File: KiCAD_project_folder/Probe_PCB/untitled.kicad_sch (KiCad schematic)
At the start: 10 parts, among them U1 LTC2452ITS8-TRMPBF, U2 BMI160

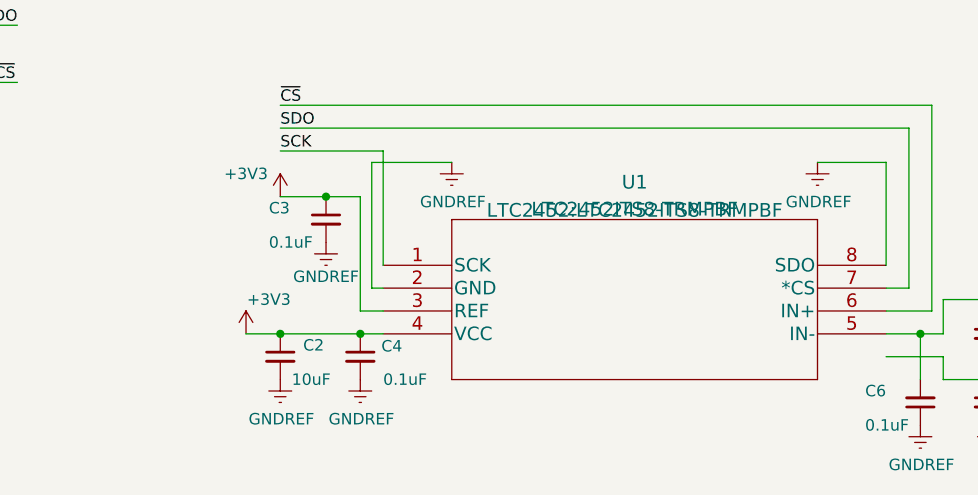
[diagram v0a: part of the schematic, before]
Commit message: Added draft PCB layout for probe
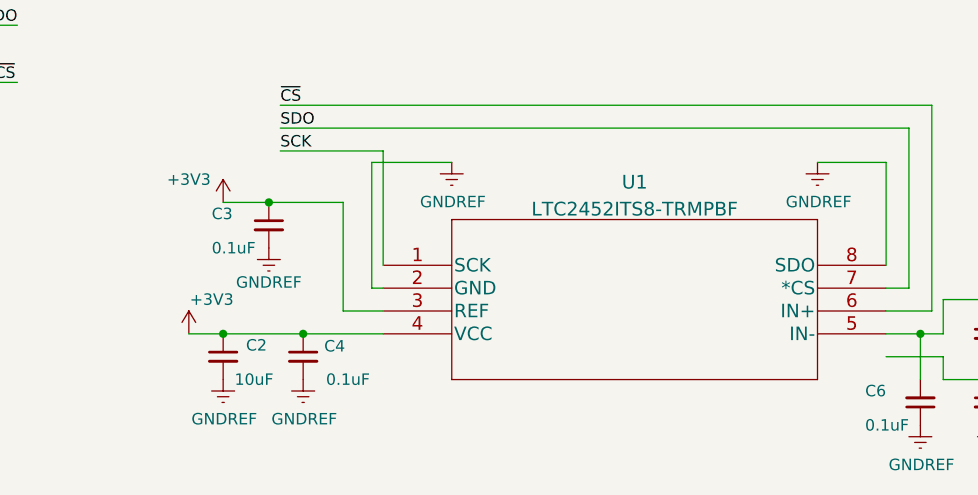
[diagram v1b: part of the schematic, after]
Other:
- moved on the sheet: C2, C3, C4

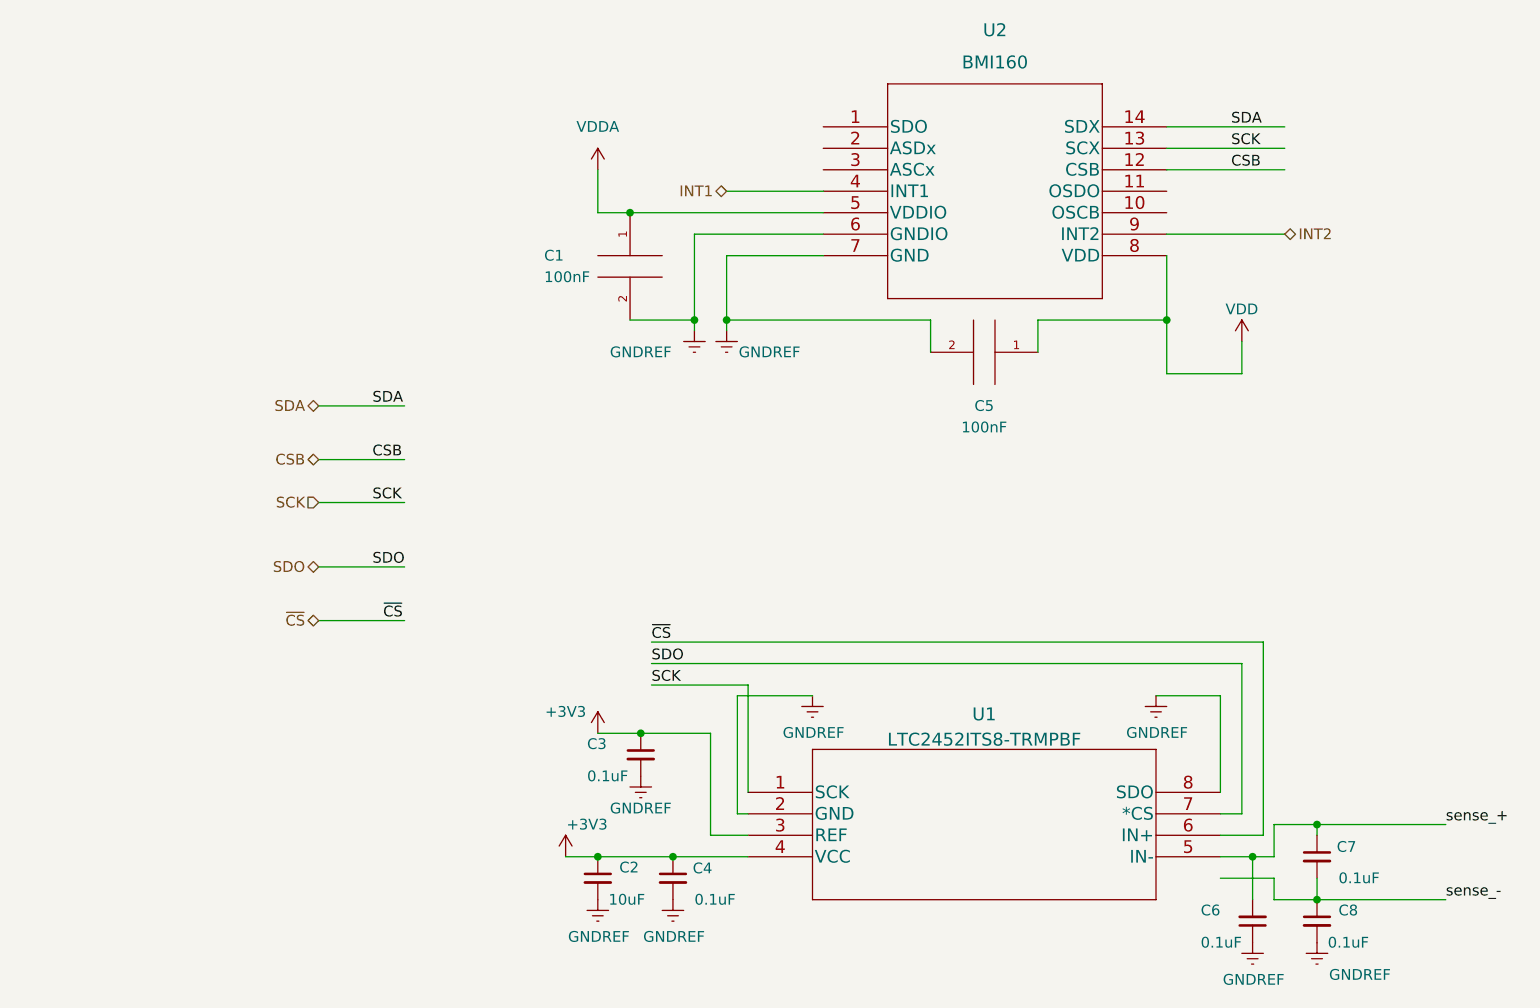
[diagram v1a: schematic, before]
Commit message: Added connector for probe, needs to be routed
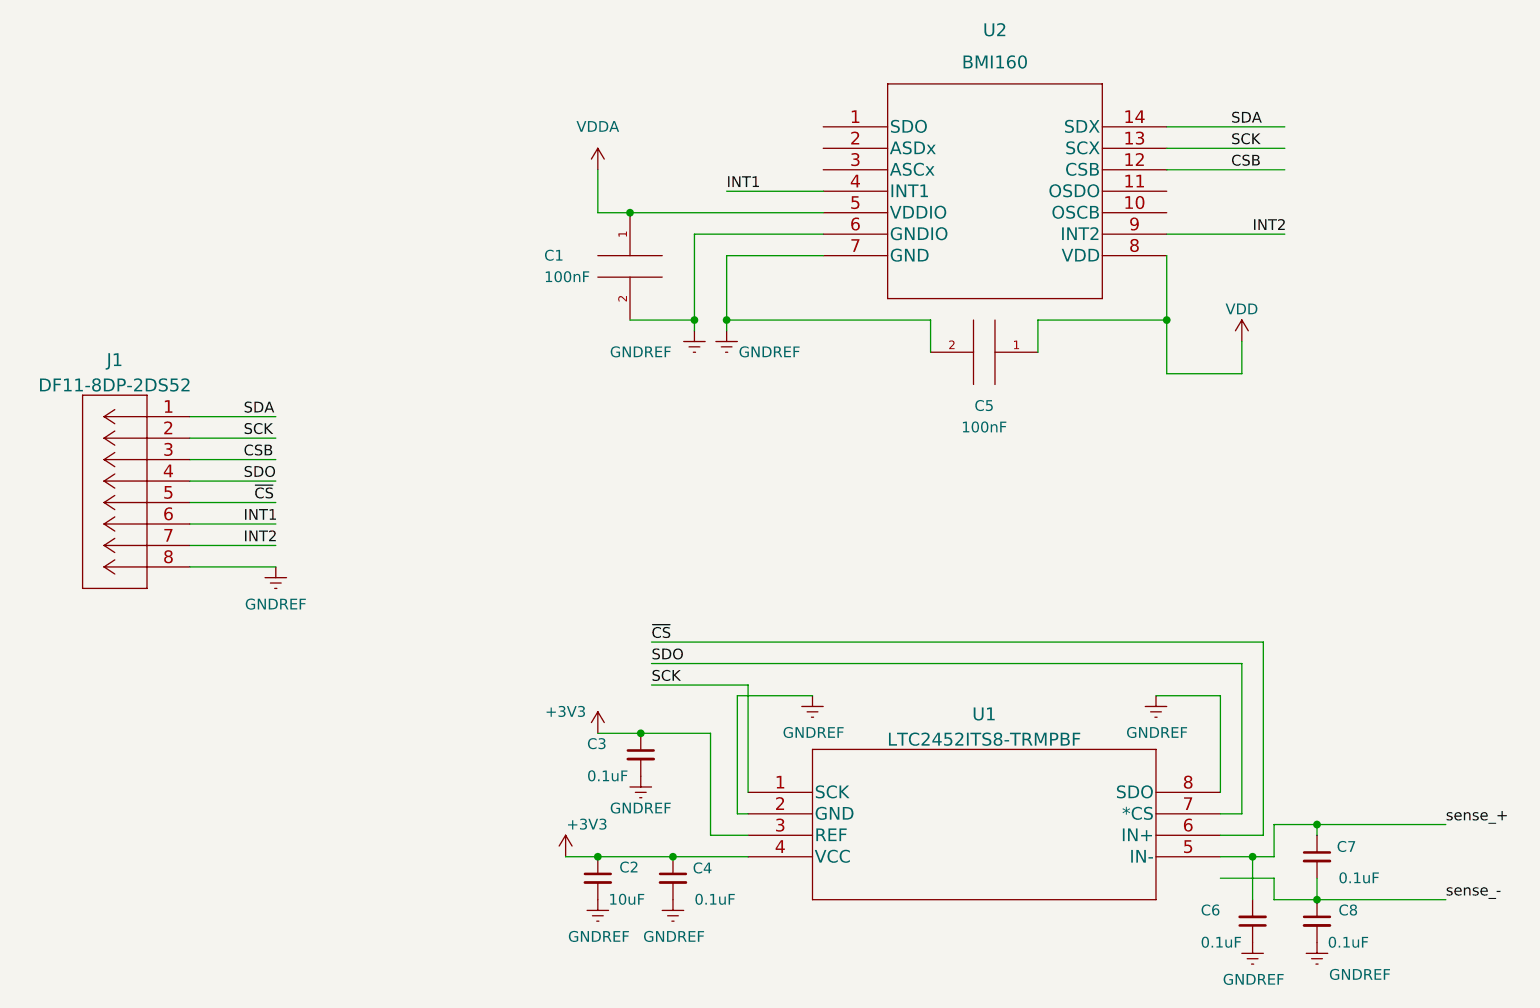
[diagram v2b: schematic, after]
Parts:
- added J1: DF11-8DP-2DS52, DF11-8POS:DF11-8DP-2DS52, symbol DF11-8POS:DF11-8DP-2DS52
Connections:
- net CSB: now also J1.3
- net GNDREF: now also J1.8
- net INT1: now also J1.6
- net INT2: now also J1.7
- net SCK: now also J1.2
- net SDA: now also J1.1
- net SDO: now also J1.4
- net ~{CS}: now also J1.5
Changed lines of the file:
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@@
     (stroke (width 0) (type default) (color 0 0 0 0))
   )
-  (wire (pts (xy 58.42 76.2) (xy 68.58 76.2))
+  (wire (pts (xy 43.18 76.2) (xy 53.34 76.2))
     (stroke (width 0) (type default) (color 0 0 0 0))
   )
@@
     (stroke (width 0) (type default) (color 0 0 0 0))
   )
-  (wire (pts (xy 58.42 81.28) (xy 68.58 81.28))
+  (wire (pts (xy 43.18 73.66) (xy 53.34 73.66))
     (stroke (width 0) (type default) (color 0 0 0 0))
   )
@@
     (stroke (width 0) (type default) (color 0 0 0 0))
   )
+  (wire (pts (xy 43.18 88.9) (xy 53.34 88.9))
+    (stroke (width 0) (type default) (color 0 0 0 0))
+  )
+  (wire (pts (xy 43.18 86.36) (xy 53.34 86.36))
+    (stroke (width 0) (type default) (color 0 0 0 0))
+  )
   (wire (pts (xy 167.64 100.33) (xy 97.79 100.33))
     (stroke (width 0) (type default) (color 0 0 0 0))
@@
     (stroke (width 0) (type default) (color 0 0 0 0))
   )
-  (wire (pts (xy 58.42 95.25) (xy 68.58 95.25))
+  (wire (pts (xy 43.18 81.28) (xy 53.34 81.28))
     (stroke (width 0) (type default) (color 0 0 0 0))
   )
@@
     (stroke (width 0) (type default) (color 0 0 0 0))
   )
-  (wire (pts (xy 58.42 69.85) (xy 68.58 69.85))
-    (stroke (width 0) (type default) (color 0 0 0 0))
-  )
-  (wire (pts (xy 58.42 88.9) (xy 68.58 88.9))
+  (wire (pts (xy 43.18 71.12) (xy 53.34 71.12))
+    (stroke (width 0) (type default) (color 0 0 0 0))
+  )
+  (wire (pts (xy 43.18 78.74) (xy 53.34 78.74))
+    (stroke (width 0) (type default) (color 0 0 0 0))
+  )
+  (wire (pts (xy 43.18 83.82) (xy 53.34 83.82))
     (stroke (width 0) (type default) (color 0 0 0 0))
   )
@@
     (stroke (width 0) (type default) (color 0 0 0 0))
   )
+  (label "INT2" (at 168.91 49.53 0)
+    (effects (font (size 1.27 1.27)) (justify left bottom))
+  )
   (label "SCK" (at 97.79 102.87 0)
     (effects (font (size 1.27 1.27)) (justify left bottom))
   )
+  (label "INT2" (at 49.53 86.36 0)
+    (effects (font (size 1.27 1.27)) (justify left bottom))
+  )
+  (label "INT1" (at 49.53 83.82 0)
+    (effects (font (size 1.27 1.27)) (justify left bottom))
+  )
   (label "sense_-" (at 191.77 128.27 0)
     (effects (font (size 1.27 1.27)) (justify left bottom))
   )
-  (label "CSB" (at 64.77 76.2 0)
+  (label "CSB" (at 49.53 76.2 0)
     (effects (font (size 1.27 1.27)) (justify left bottom))
   )
@@
     (effects (font (size 1.27 1.27)) (justify left bottom))
   )
-  (label "SDA" (at 64.77 69.85 0)
+  (label "SDA" (at 49.53 71.12 0)
     (effects (font (size 1.27 1.27)) (justify left bottom))
   )
@@
     (effects (font (size 1.27 1.27)) (justify left bottom))
   )
-  (label "SCK" (at 64.77 81.28 0)
+  (label "SCK" (at 49.53 73.66 0)
     (effects (font (size 1.27 1.27)) (justify left bottom))
   )
@@
     (effects (font (size 1.27 1.27)) (justify left bottom))
   )
-  (label "~{CS}" (at 66.04 95.25 0)
-    (effects (font (size 1.27 1.27)) (justify left bottom))
-  )
-  (label "SDO" (at 64.77 88.9 0)
+  (label "~{CS}" (at 50.8 81.28 0)
+    (effects (font (size 1.27 1.27)) (justify left bottom))
+  )
+  (label "SDO" (at 49.53 78.74 0)
     (effects (font (size 1.27 1.27)) (justify left bottom))
   )
@@
     (effects (font (size 1.27 1.27)) (justify left bottom))
   )
-  (hierarchical_label "INT2" (shape bidirectional) (at 172.72 49.53 0)
-    (effects (font (size 1.27 1.27)) (justify left))
-  )
-  (hierarchical_label "CSB" (shape bidirectional) (at 58.42 76.2 180)
-    (effects (font (size 1.27 1.27)) (justify right))
-  )
-  (hierarchical_label "SCK" (shape input) (at 58.42 81.28 180)
-    (effects (font (size 1.27 1.27)) (justify right))
-  )
-  (hierarchical_label "~{CS}" (shape bidirectional) (at 58.42 95.25 180)
-    (effects (font (size 1.27 1.27)) (justify right))
-  )
-  (hierarchical_label "INT1" (shape bidirectional) (at 106.68 44.45 180)
-    (effects (font (size 1.27 1.27)) (justify right))
-  )
-  (hierarchical_label "SDA" (shape bidirectional) (at 58.42 69.85 180)
-    (effects (font (size 1.27 1.27)) (justify right))
-  )
-  (hierarchical_label "SDO" (shape bidirectional) (at 58.42 88.9 180)
-    (effects (font (size 1.27 1.27)) (justify right))
+  (label "INT1" (at 106.68 44.45 0)
+    (effects (font (size 1.27 1.27)) (justify left bottom))
   )
   (symbol (lib_id "power:VDD") (at 167.64 62.23 0) (unit 1)
@@
     )
     (property "Datasheet" "" (id 3) (at 176.53 133.35 0)
+      (effects (font (size 1.27 1.27)) hide)
+    )
+    (pin "1")
+  )
+  (symbol (lib_id "power:GNDREF") (at 53.34 88.9 0) (unit 1)
+    (in_bom yes) (on_board yes) (fields_autoplaced)
+    (property "Reference" "#PWR0101" (id 0) (at 53.34 95.25 0)
+      (effects (font (size 1.27 1.27)) hide)
+    )
+    (property "Value" "GNDREF" (id 1) (at 53.34 93.3434 0))
+    (property "Footprint" "" (id 2) (at 53.34 88.9 0)
+      (effects (font (size 1.27 1.27)) hide)
+    )
+    (property "Datasheet" "" (id 3) (at 53.34 88.9 0)
       (effects (font (size 1.27 1.27)) hide)
     )
@@
     (pin "1")
   )
+  (symbol (lib_id "DF11-8POS:DF11-8DP-2DS52") (at 43.18 71.12 0) (mirror y) (unit 1)
+    (in_bom yes) (on_board yes) (fields_autoplaced)
+    (property "Reference" "J1" (id 0) (at 34.29 64.4324 0)
+      (effects (font (size 1.524 1.524)))
+    )
+    (property "Value" "DF11-8DP-2DS52" (id 1) (at 34.29 67.4258 0)
+      (effects (font (size 1.524 1.524)))
+    )
+    (property "Footprint" "DF11-8POS:DF11-8DP-2DS52" (id 2) (at 33.02 82.804 0)
+      (effects (font (size 1.524 1.524)) hide)
+    )
+    (property "Datasheet" "" (id 3) (at 43.18 71.12 0)
+      (effects (font (size 1.524 1.524)))
+    )
+    (pin "1")
+    (pin "2")
+    (pin "3")
+    (pin "4")
+    (pin "5")
+    (pin "6")
+    (pin "7")
+    (pin "8")
+  )
   (symbol (lib_id "power:+3V3") (at 87.63 123.19 0) (unit 1)
